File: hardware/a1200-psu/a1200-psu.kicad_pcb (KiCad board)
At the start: 2 copper layers, 147 x 76 mm, 61 parts, among them J1 AC-In, J2 DC-Out, Q1 P2N60, U1 UC3844_DIP8, U2 PC817, U3 TL431D

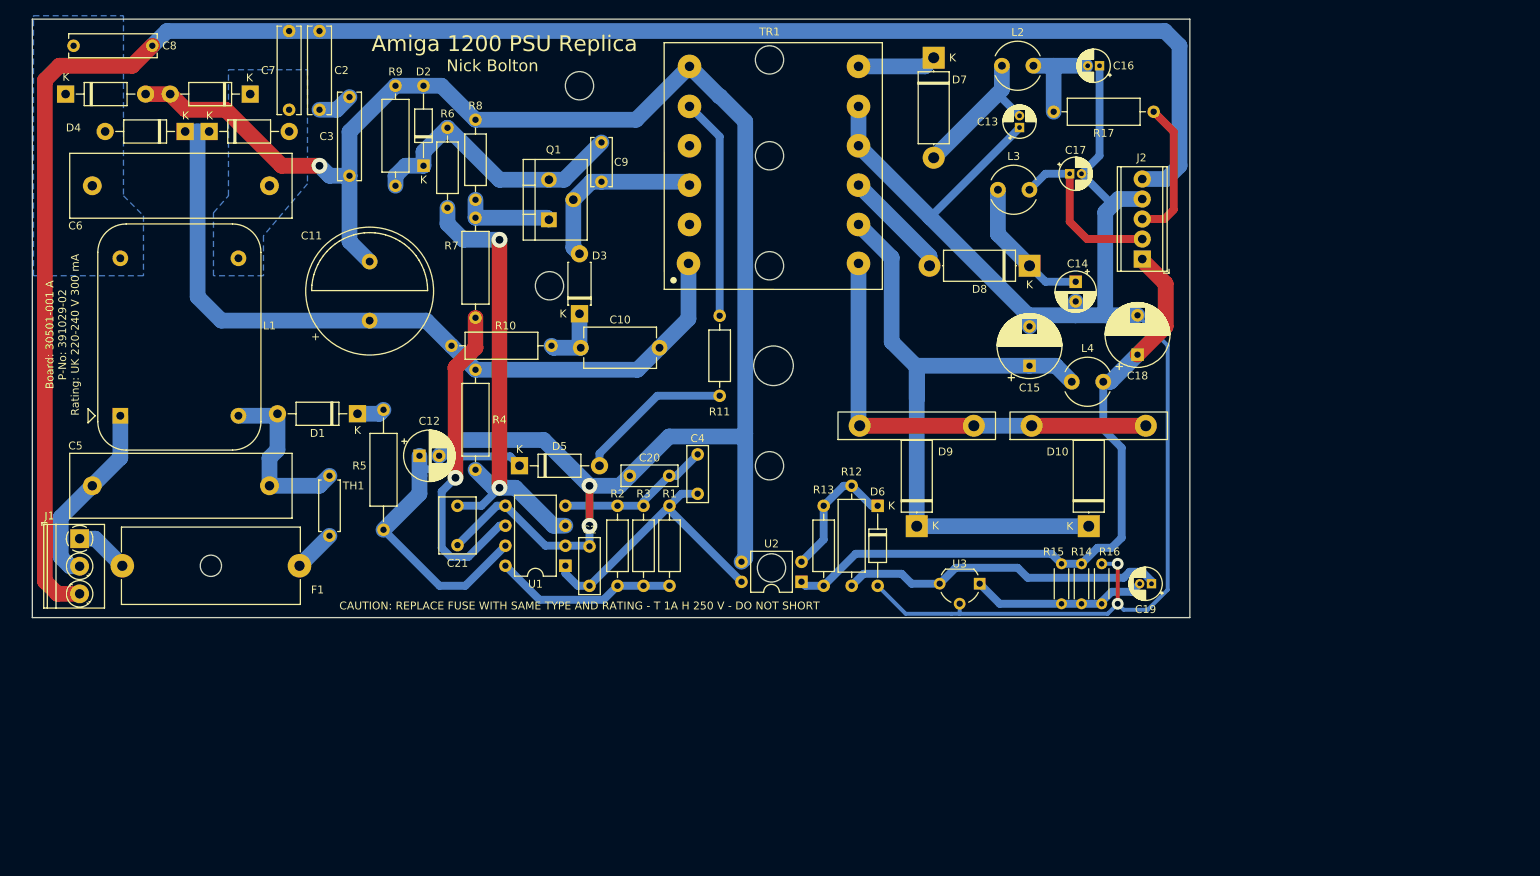
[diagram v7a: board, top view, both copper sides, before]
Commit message: Update 3D model pos
Also add jumper from original; not required for circuit but helps to understand the original board
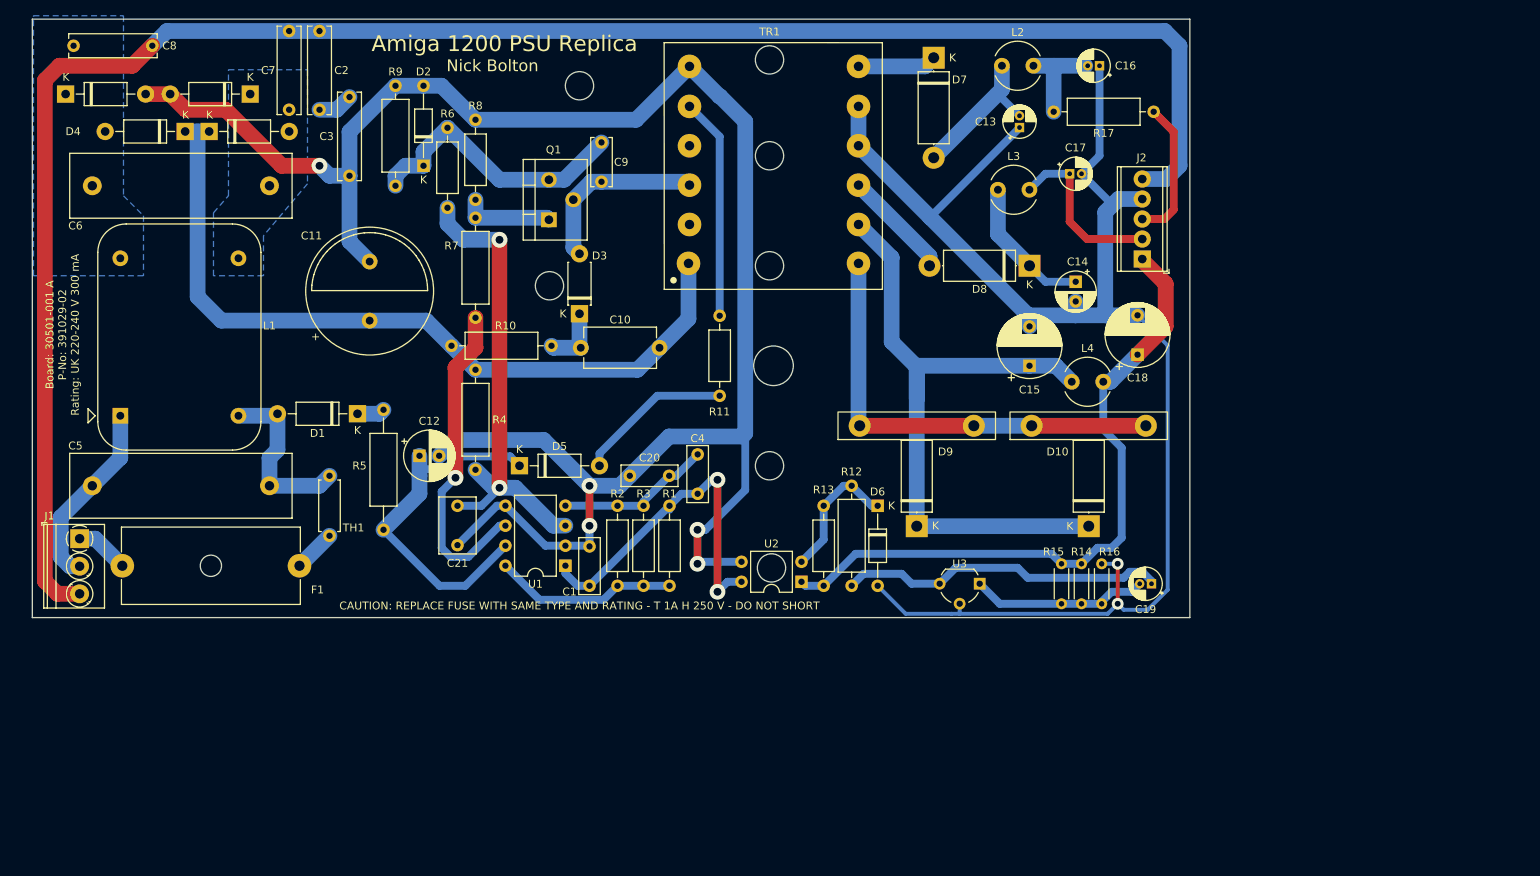
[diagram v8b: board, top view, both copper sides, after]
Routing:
- net GNDD: track 237.4 -> 246.3 mm, vias 3 -> 5
- net Net-(C1-Pad2): track 36.7 -> 44.8 mm, vias 0 -> 2
